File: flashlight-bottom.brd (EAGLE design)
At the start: 33.1 x 17.8 mm, 0 parts

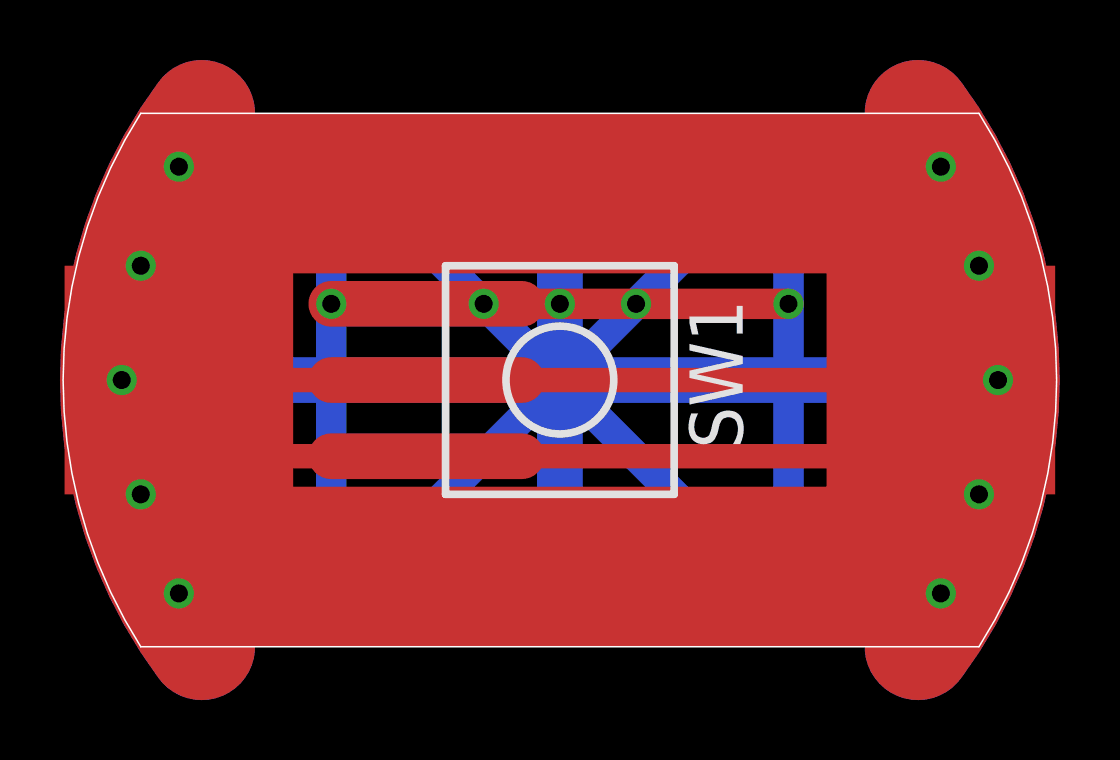
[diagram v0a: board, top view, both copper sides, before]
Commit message: add stockton logo to solder mask
add thermal mask to top
replace rhs of top with curved wire

label pins of switch on bottom
reduce size of tab solder area
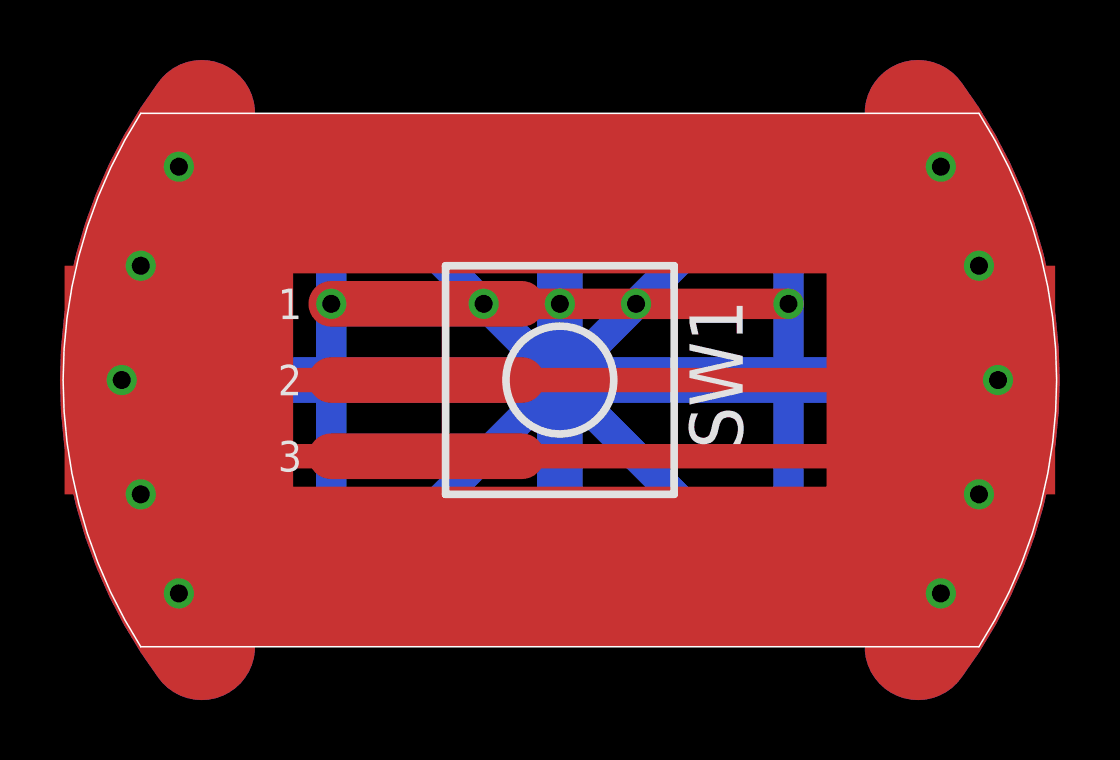
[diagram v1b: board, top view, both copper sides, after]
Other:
- board text added: "1"
- board text added: "2"
- board text added: "3"
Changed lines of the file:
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@@
 <circle x="16.51" y="8.89" radius="6.35" width="0.254" layer="22"/>
 <rectangle x1="25.4" y1="5.08" x2="33.02" y2="12.7" layer="1"/>
-<rectangle x1="25.4" y1="5.08" x2="33.02" y2="12.7" layer="29"/>
-<rectangle x1="0" y1="5.08" x2="7.62" y2="12.7" layer="29"/>
+<rectangle x1="26.67" y1="5.08" x2="33.02" y2="12.7" layer="29"/>
+<rectangle x1="0" y1="5.08" x2="6.35" y2="12.7" layer="29"/>
 <rectangle x1="0" y1="5.08" x2="7.62" y2="12.7" layer="1"/>
 <wire x1="2.54" y1="17.78" x2="2.54" y2="0" width="0.0508" layer="20" curve="64.94"/>
@@
 <text x="7.62" y="15.748" size="1.016" layer="22" rot="MR270"> 3x C  battery
  This  end (-)</text>
+<text x="7.112" y="10.922" size="1.016" layer="25">1</text>
+<text x="7.112" y="8.382" size="1.016" layer="25">2</text>
+<text x="7.112" y="5.842" size="1.016" layer="25">3</text>
+<wire x1="25.146" y1="14.732" x2="25.146" y2="15.748" width="0.4064" layer="29"/>
+<wire x1="25.146" y1="15.748" x2="24.384" y2="16.51" width="0.4064" layer="29"/>
+<wire x1="25.146" y1="15.748" x2="25.908" y2="16.51" width="0.4064" layer="29"/>
+<wire x1="26.67" y1="14.732" x2="26.67" y2="15.748" width="0.4064" layer="29"/>
+<wire x1="26.67" y1="15.748" x2="25.908" y2="16.51" width="0.4064" layer="29"/>
+<wire x1="26.67" y1="15.748" x2="27.432" y2="16.51" width="0.4064" layer="29"/>
+<wire x1="24.384" y1="17.018" x2="27.432" y2="17.018" width="0.4064" layer="29" curve="-36.846038"/>
 </plain>
 <attributes>
